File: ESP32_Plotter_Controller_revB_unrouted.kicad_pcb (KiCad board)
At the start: 2 copper layers, 99.1 x 55.4 mm, 49 parts, among them J1 JTAG, J10 Pen Lift, J11 5v Vin, J12 X Motor, J13 Y Motor, J14 NEOPIXEL, J15 Pen Dir, J16 Aux Port (I2C), J17 USB, J18 E-Stop, J19 Y Limit, J2 Power (12v), J3 5V Aux, J4 Vin Aux, J5 X Limit, J6 Aux Port (SPI), J7 X Limit, J8 Micro_SD_Card, J9 Y Limit, SW1 RESET, SW2 BOOT, U1 ESP32-WROOM-32D, U2 TMC2130, U3 TMC2130, U4 XL1509, U5 CH340C, U6 AMS1117-3.3

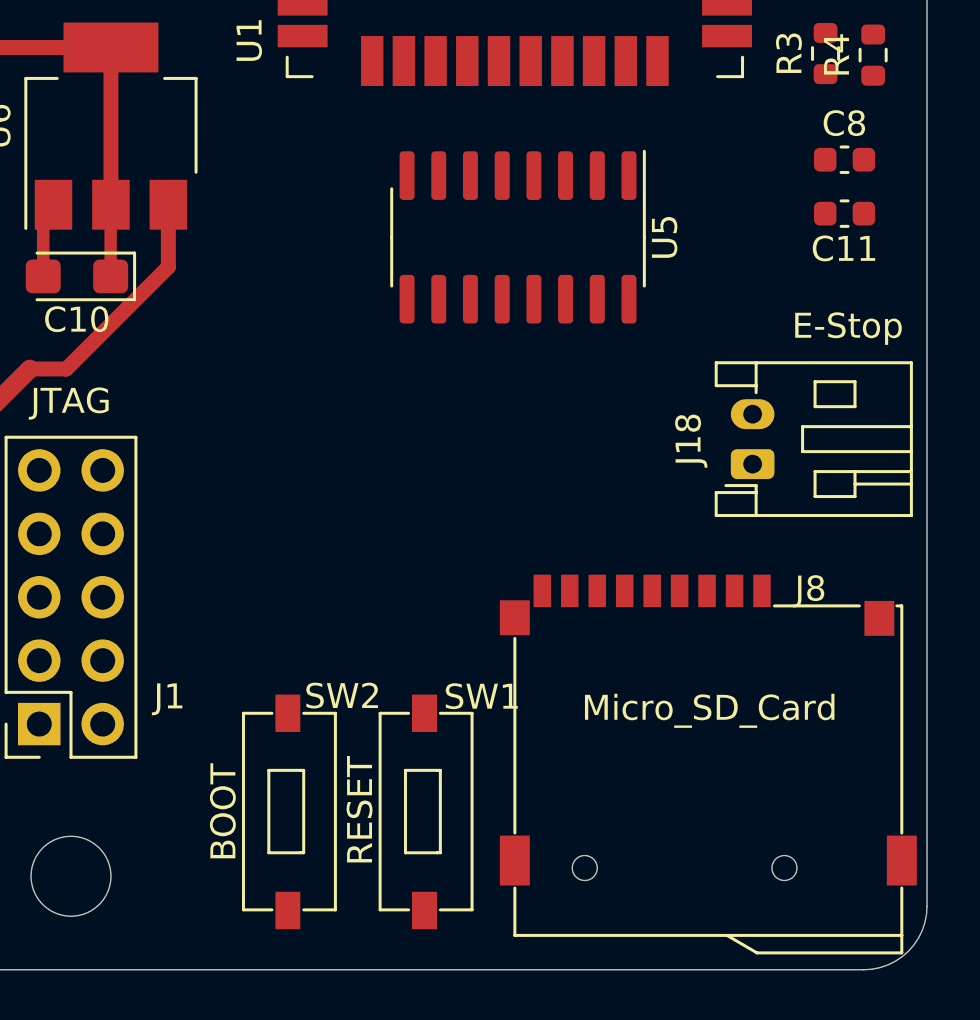
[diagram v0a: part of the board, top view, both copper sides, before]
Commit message: Tweaked component layout again
Moved buttons, sdcard and usb chip around
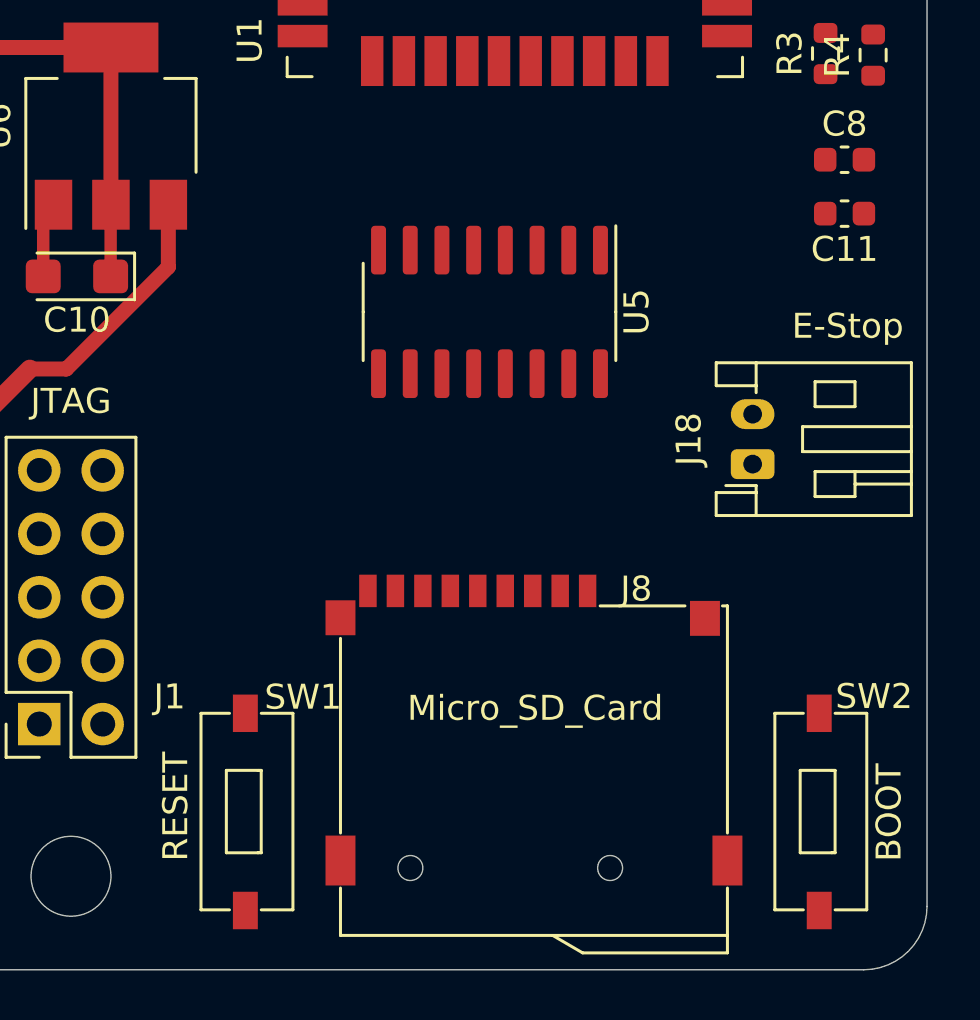
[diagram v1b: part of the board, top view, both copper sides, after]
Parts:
- moved SW2 21.3 mm to (120.1, 114.1)
- moved SW1 7.18 mm to (97.2, 114.1)
- moved J8 6.98 mm to (101.0, 109.2)
- moved U5 3.20 mm to (106.9, 98.0)

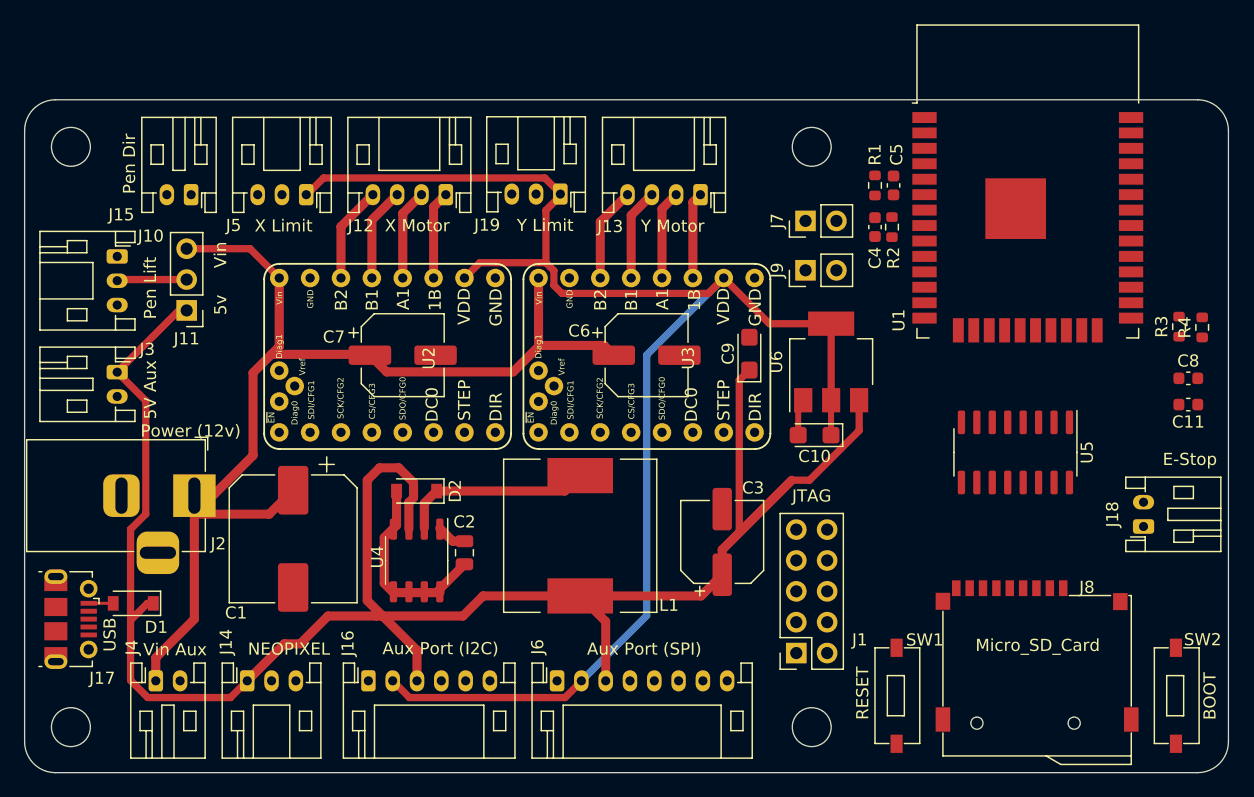
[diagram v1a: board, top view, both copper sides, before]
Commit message: Change to USB C connector
Had to move connectors around to make room.
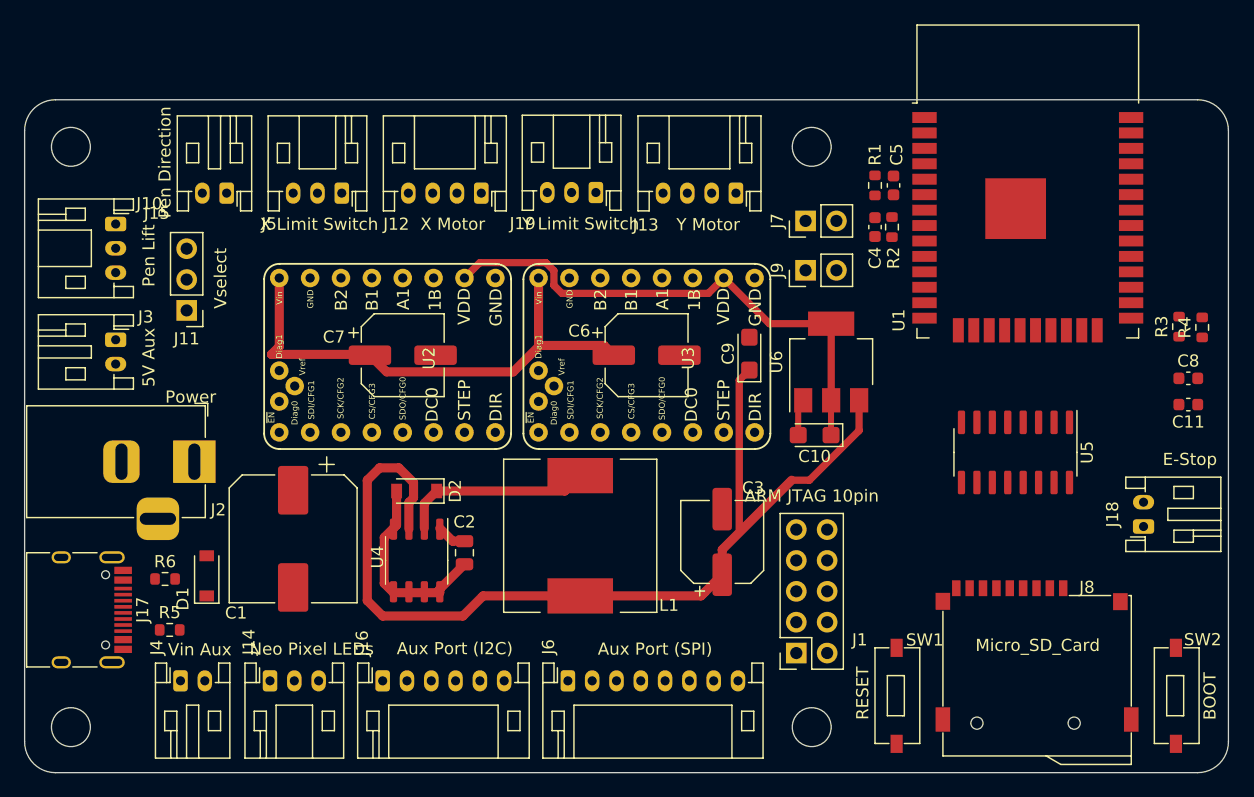
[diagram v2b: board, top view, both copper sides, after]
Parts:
- added R5: 5.1k, Resistor_SMD:R_0603_1608Metric, F.Cu at (37.3, 112.6)
- added R6: 5.1k, Resistor_SMD:R_0603_1608Metric, F.Cu at (37.0, 108.5)
- J1: value JTAG -> ARM JTAG 10pin
- J11: value 5v Vin -> Vselect
- J14: value NEOPIXEL -> Neo Pixel LEDs
- J15: value Pen Dir -> Pen Direction
- J17: value USB -> USB_C_Receptacle_USB2.0; footprint Connector_USB:USB_Micro-B_Molex-105017-0001 -> Connector_USB:USB_C_Receptacle_HRO_TYPE-C-31-M-12
- J19: value Y Limit -> Y Limit Switch
- J2: value Power (12v) -> Power
- J5: value X Limit -> X Limit Switch
- moved D1 6.45 mm to (40.4, 108.2), turned to 90 degrees
- moved J19 2.92 mm to (72.4, 76.7)
- moved J12 2.92 mm to (63.0, 76.7)
- moved J15 2.92 mm to (42.0, 76.7)
- moved J5 2.92 mm to (51.5, 76.7)
- moved J13 2.92 mm to (83.9, 76.7)
- moved J2 2.79 mm to (39.4, 98.8)
- moved J10 2.67 mm to (32.9, 79.2)
- moved J3 2.67 mm to (32.9, 88.8)
- moved J4 2.03 mm to (38.2, 116.8)
- moved J14 1.87 mm to (45.6, 116.8)
- moved J16 1.17 mm to (54.9, 116.8)
- moved J6 0.89 mm to (70.1, 116.8)
- moved J17 0.80 mm to (29.5, 111.0)
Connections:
- U5 pad 5: Net-(J17-Pad3) -> Net-(J17-PadA6)
- U5 pad 6: Net-(J17-Pad2) -> Net-(J17-PadA7)
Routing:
- net +3V3: track 126.6 -> 43.7 mm
- net +5V: track 160.9 -> 85.4 mm
- net /Vin: track 93.0 -> 44.6 mm
- net Net-(J12-Pad4): track 7.94 -> 0.00 mm
- net Net-(J13-Pad4): track 7.79 -> 0.00 mm
- net Net-(J12-Pad3): track 7.72 -> 0.00 mm
- net Net-(J13-Pad3): track 7.56 -> 0.00 mm
- net Net-(J12-Pad2): track 7.50 -> 0.00 mm
- net Net-(J13-Pad2): track 7.34 -> 0.00 mm
- net Net-(J12-Pad1): track 7.27 -> 0.00 mm
- net Net-(J13-Pad1): track 7.12 -> 0.00 mm
- net Net-(J10-Pad2): track 5.75 -> 0.00 mm
- net Net-(D1-Pad2): track 2.02 -> 0.00 mm
